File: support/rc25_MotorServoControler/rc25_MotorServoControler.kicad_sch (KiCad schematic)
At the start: 23 parts, among them J1 Conn_01x03_Pin, Q1 Q_NPN, Q2 Q_NPN, Q3 Q_NPN, SW1 SW_SPST, SW2 SW_SPST, SW3 SW_SPST, U1 RP2040-Zero, U3 CD4066

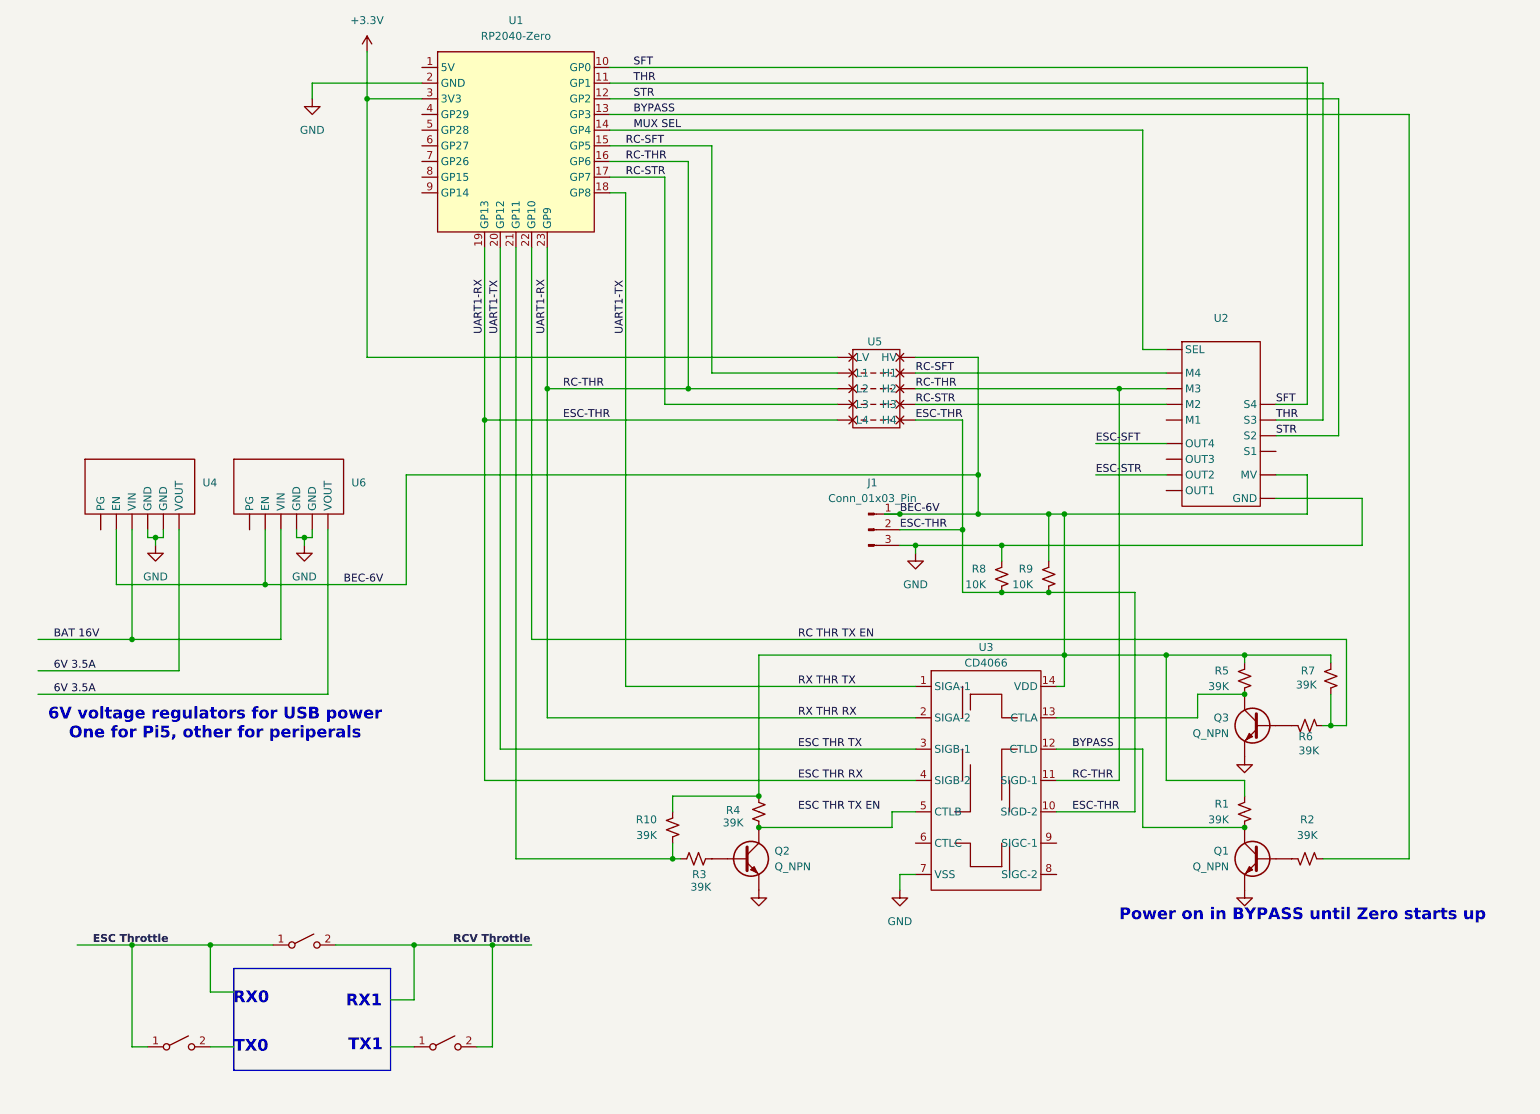
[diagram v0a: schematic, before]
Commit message: added engine schematic and mucked with engine code bypass and passthrough work with Telemetry going to the transmitter
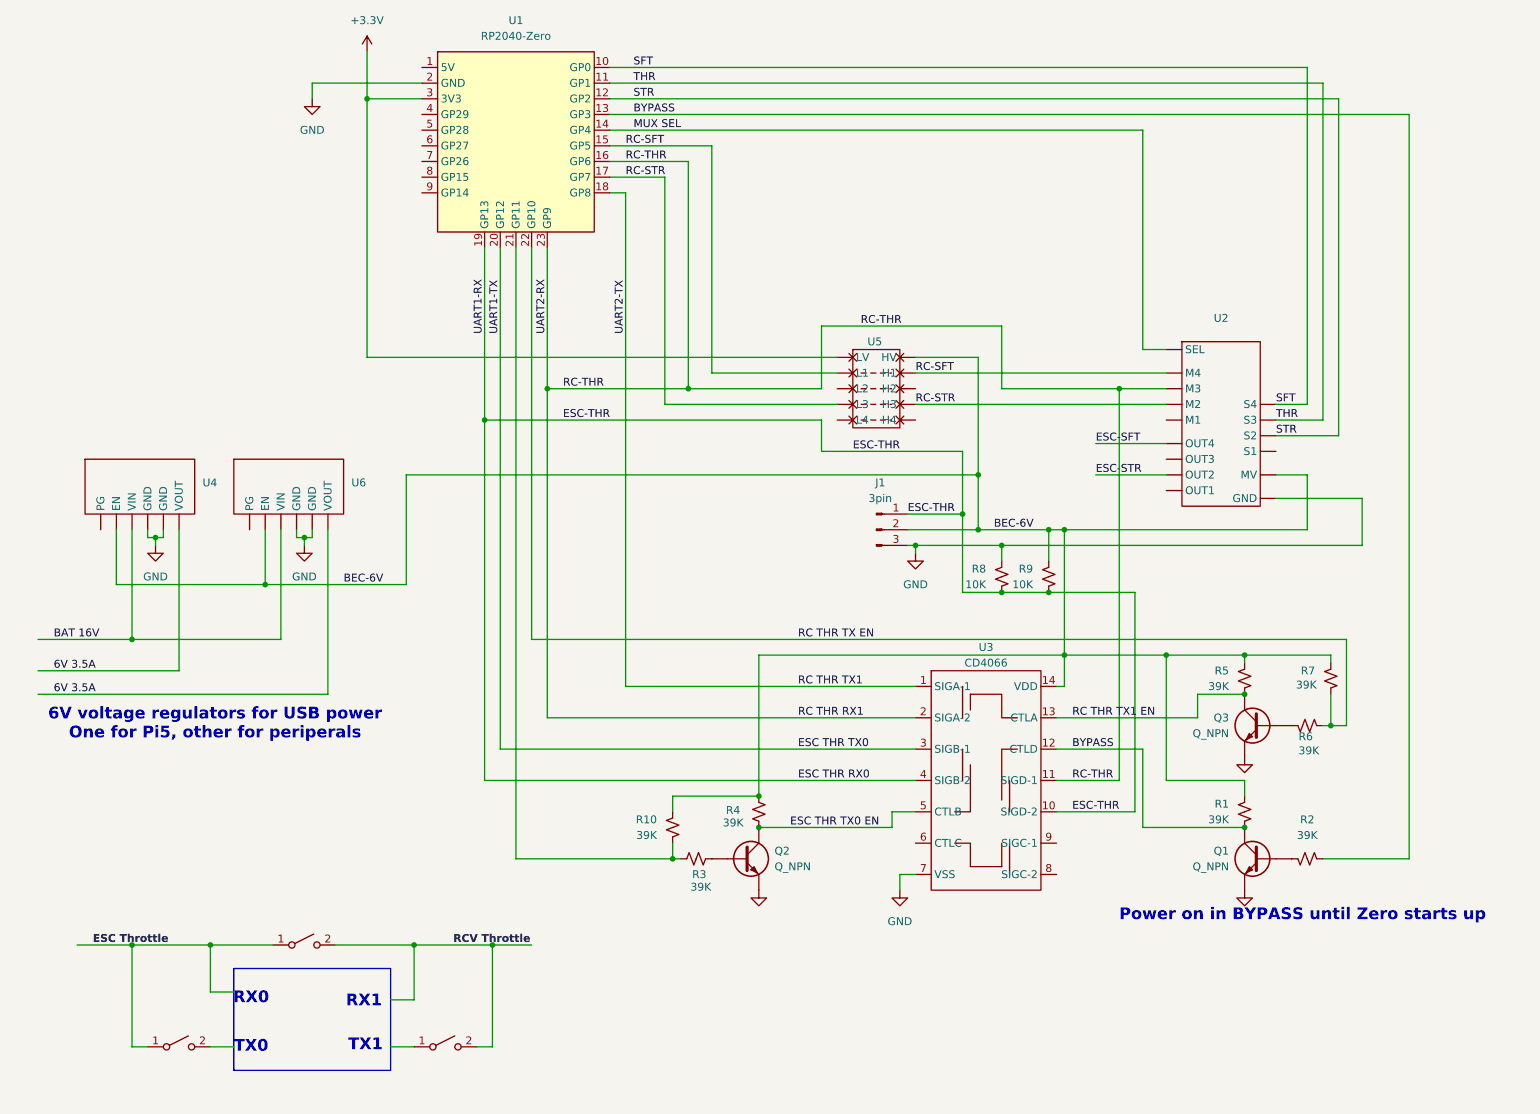
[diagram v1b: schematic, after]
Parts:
- J1: value Conn_01x03_Pin -> 3pin
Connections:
- net BEC-6V: now also J1.2 (Pin_2); no longer J1.1 (Pin_1)
- net RC THR TX1 EN: now reaches Q3.C, R5.2, U3.13 (CTLA)
- net ESC THR TX0 EN: now reaches Q2.C, R4.2, U3.5 (CTLB)
- removed net ESC THR RX: J1.2 (Pin_2), R8.2, R9.2, U1.16 (GP6), U1.19 (GP13), U1.23 (GP9), U2. (GND), U3.10 (SIGD-2), U3.11 (SIGD-1), U3.2 (SIGA-2), U3.4 (SIGB-2), U5. (H4)
- net ESC THR TX renamed ESC THR TX0
- net ESC THR TX0: no longer U1.18 (GP8), U3.1 (SIGA-1)
- new net ESC THR RX0: J1.1 (Pin_1), R8.2, R9.2, U1.19 (GP13), U3.10 (SIGD-2), U3.4 (SIGB-2)
- new net RC THR RX1: U1.16 (GP6), U1.23 (GP9), U2. (GND), U3.11 (SIGD-1), U3.2 (SIGA-2)
- new net RC THR TX1: U1.18 (GP8), U3.1 (SIGA-1)
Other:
- moved on the sheet: J1

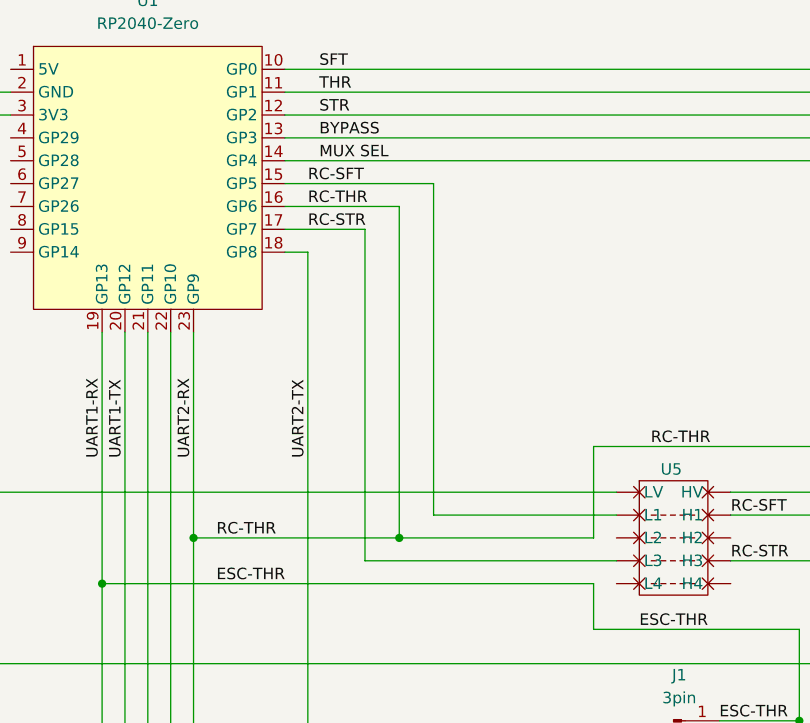
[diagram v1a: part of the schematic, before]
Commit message: mSteer and mShift pins were swapped (the board wiring of these pins must have accidently changed during SRXL2 updates) Crude passthru OK: throttle  RXCL2 steer,shift PWM
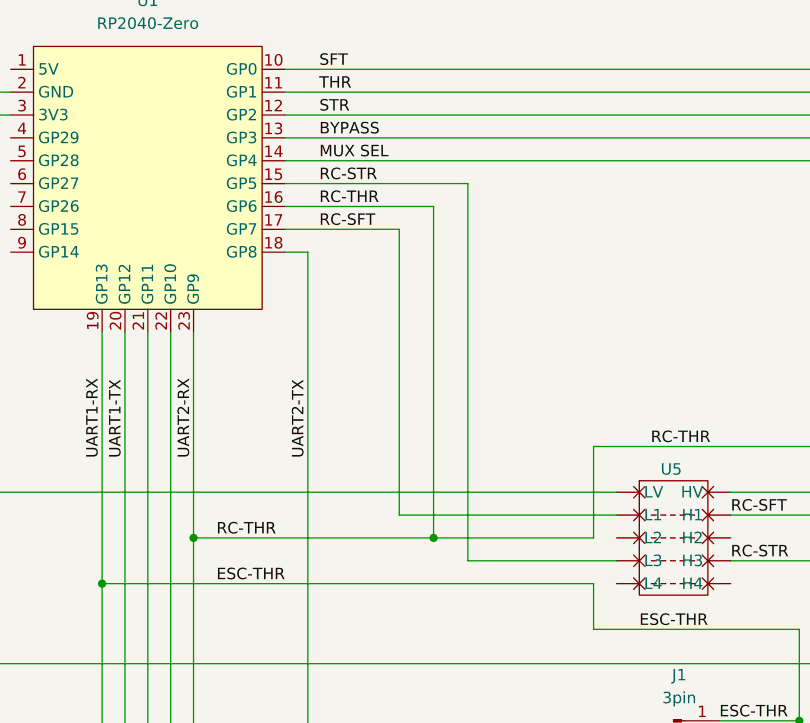
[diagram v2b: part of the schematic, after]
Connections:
- net RC-SFT: now also U1.17 (GP7); no longer U1.15 (GP5)
- net RC-STR: now also U1.15 (GP5); no longer U1.17 (GP7)
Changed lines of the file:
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@@
-	)
-	(junction
-		(at 123.19 77.47)
-		(diameter 0)
-		(color 0 0 0 0)
 	)
 	(junction
@@
 	)
 	(junction
+		(at 127 77.47)
+		(diameter 0)
+		(color 0 0 0 0)
+	)
+	(junction
 		(at 181.61 110.49)
 		(diameter 0)
@@
 	(wire
 		(pts
+			(xy 130.81 38.1) (xy 130.81 80.01)
+		)
+		(stroke
+			(width 0)
+			(type default)
+		)
+	)
+	(wire
+		(pts
 			(xy 71.12 30.48) (xy 80.01 30.48)
 		)
@@
 	(wire
 		(pts
-			(xy 119.38 43.18) (xy 119.38 80.01)
-		)
-		(stroke
-			(width 0)
-			(type default)
-		)
-	)
-	(wire
-		(pts
 			(xy 62.23 27.94) (xy 80.01 27.94)
 		)
@@
 	(wire
 		(pts
+			(xy 130.81 80.01) (xy 147.32 80.01)
+		)
+		(stroke
+			(width 0)
+			(type default)
+		)
+	)
+	(wire
+		(pts
 			(xy 36.83 101.6) (xy 36.83 102.87)
 		)
@@
 	(wire
 		(pts
+			(xy 123.19 43.18) (xy 123.19 74.93)
+		)
+		(stroke
+			(width 0)
+			(type default)
+		)
+	)
+	(wire
+		(pts
 			(xy 54.61 109.22) (xy 77.47 109.22)
 		)
@@
 	(wire
 		(pts
-			(xy 110.49 43.18) (xy 119.38 43.18)
+			(xy 110.49 43.18) (xy 123.19 43.18)
 		)
 		(stroke
@@
 	(wire
 		(pts
+			(xy 123.19 74.93) (xy 147.32 74.93)
+		)
+		(stroke
+			(width 0)
+			(type default)
+		)
+	)
+	(wire
+		(pts
 			(xy 134.62 148.59) (xy 156.21 148.59)
 		)
@@
 	(wire
 		(pts
-			(xy 123.19 77.47) (xy 100.33 77.47)
+			(xy 100.33 77.47) (xy 127 77.47)
 		)
 		(stroke
@@
 	(wire
 		(pts
-			(xy 123.19 77.47) (xy 144.78 77.47)
-		)
-		(stroke
-			(width 0)
-			(type default)
-		)
-	)
-	(wire
-		(pts
 			(xy 134.62 120.65) (xy 134.62 143.51)
 		)
@@
 	(wire
 		(pts
+			(xy 127 77.47) (xy 144.78 77.47)
+		)
+		(stroke
+			(width 0)
+			(type default)
+		)
+	)
+	(wire
+		(pts
 			(xy 189.23 91.44) (xy 200.66 91.44)
 		)
@@
 	(wire
 		(pts
-			(xy 123.19 40.64) (xy 123.19 77.47)
+			(xy 127 40.64) (xy 127 77.47)
 		)
 		(stroke
@@
 	(wire
 		(pts
-			(xy 110.49 38.1) (xy 127 38.1)
+			(xy 110.49 38.1) (xy 130.81 38.1)
 		)
 		(stroke
@@
 	(wire
 		(pts
-			(xy 119.38 80.01) (xy 147.32 80.01)
-		)
-		(stroke
-			(width 0)
-			(type default)
-		)
-	)
-	(wire
-		(pts
 			(xy 167.64 87.63) (xy 167.64 97.79)
 		)
@@
 	(wire
 		(pts
-			(xy 127 38.1) (xy 127 74.93)
-		)
-		(stroke
-			(width 0)
-			(type default)
-		)
-	)
-	(wire
-		(pts
 			(xy 95.25 153.67) (xy 120.65 153.67)
 		)
@@
 	(wire
 		(pts
-			(xy 127 74.93) (xy 147.32 74.93)
-		)
-		(stroke
-			(width 0)
-			(type default)
-		)
-	)
-	(wire
-		(pts
 			(xy 45.72 167.64) (xy 45.72 175.26)
 		)
@@
 	(wire
 		(pts
-			(xy 110.49 40.64) (xy 123.19 40.64)
+			(xy 110.49 40.64) (xy 127 40.64)
 		)
 		(stroke
@@
 		)
 	)
-	(label "RC-STR"
-		(at 113.03 43.18 0)
-		(effects
-			(font
-				(size 1.27 1.27)
-			)
-			(justify left bottom)
-		)
-	)
 	(label "UART2-TX"
 		(at 113.03 68.58 90)
@@
 		)
 	)
+	(label "RC-SFT"
+		(at 114.3 43.18 0)
+		(effects
+			(font
+				(size 1.27 1.27)
+			)
+			(justify left bottom)
+		)
+	)
 	(label "RC-STR"
 		(at 160.02 80.01 0)
@@
 	)
 	(label "RC-SFT"
-		(at 113.03 38.1 0)
-		(effects
-			(font
-				(size 1.27 1.27)
-			)
-			(justify left bottom)
-		)
-	)
-	(label "RC-SFT"
 		(at 160.02 74.93 0)
 		(effects
@@
 		)
 	)
+	(label "RC-STR"
+		(at 114.3 38.1 0)
+		(effects
+			(font
+				(size 1.27 1.27)
+			)
+			(justify left bottom)
+		)
+	)
 	(label "RC-THR"
 		(at 185.42 140.97 0)
@@
 	)
 	(label "RC-THR"
-		(at 113.03 40.64 0)
-		(effects
-			(font
+		(at 114.3 40.64 0)
+		(effects
+			(font

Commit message: added pwm headers
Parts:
- added ESC-SFT, ESC-STR, NC (x3), RCV-SFT, RCV-STR, RCV-THR: 3pin, symbol Connector:Conn_01x03_Pin
- added J2: Conn_01x04, symbol Connector_Generic:Conn_01x04
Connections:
- net +3.3V: now also J2.1 (Pin_1)
- net ESC-SFT: now also ESC-SFT.2 (Pin_2)
- net ESC-STR: now also ESC-STR.2 (Pin_2)
- net GND: now also J2.2 (Pin_2)
- net RC THR RX1: now also RCV-THR.2 (Pin_2)
- net RC-SFT: now also RCV-SFT.2 (Pin_2)
- net RC-STR: now also RCV-STR.2 (Pin_2)
- net BLU: now reaches U1.8 (GP15)
- net BLU: now also J2.3 (Pin_3)
- net WHT: now reaches U1.9 (GP14)
- net WHT: now also J2.4 (Pin_4)
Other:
- note added: "High level diagram of Throttle signals"
- note added: "Odom Pod measuring drive shaft rotation speed"
